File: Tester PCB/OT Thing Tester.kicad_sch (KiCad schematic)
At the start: 84 parts, among them J1 Conn_01x05, J2 Conn_01x08, J3 Conn_01x05, J4 Conn_01x05, J5 Link, J6 Link, Q1 BSP62, Q2 BSP62, Q3 BC847, Q4 BC847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

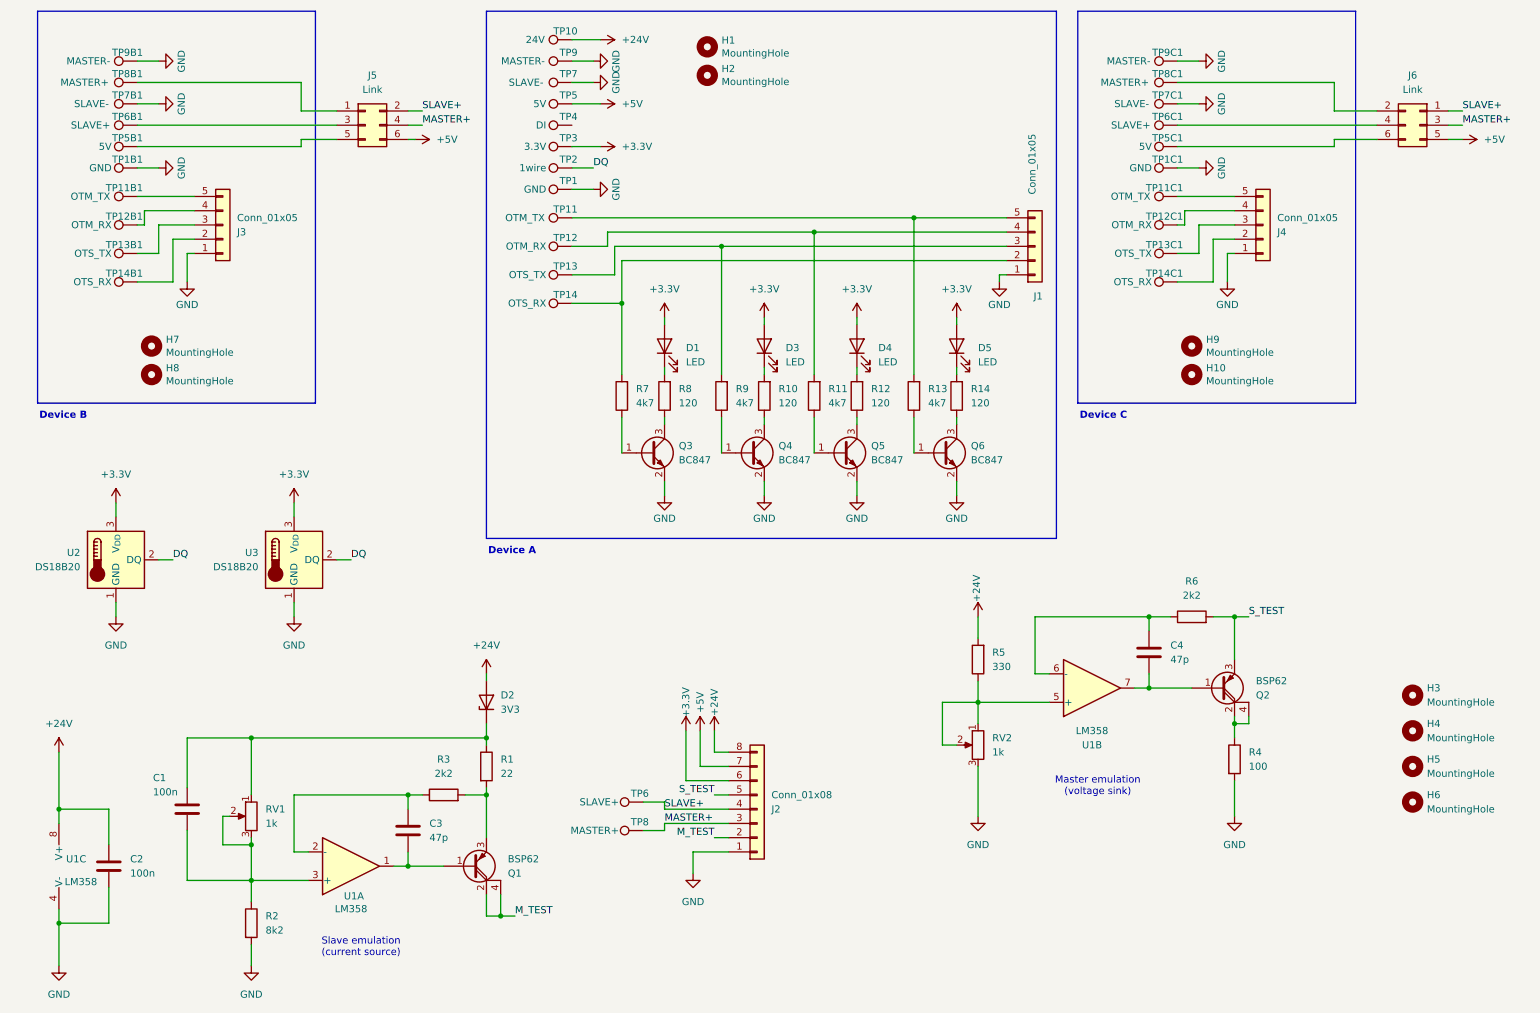
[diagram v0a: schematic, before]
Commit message: add USB test points single board test w/ power supply
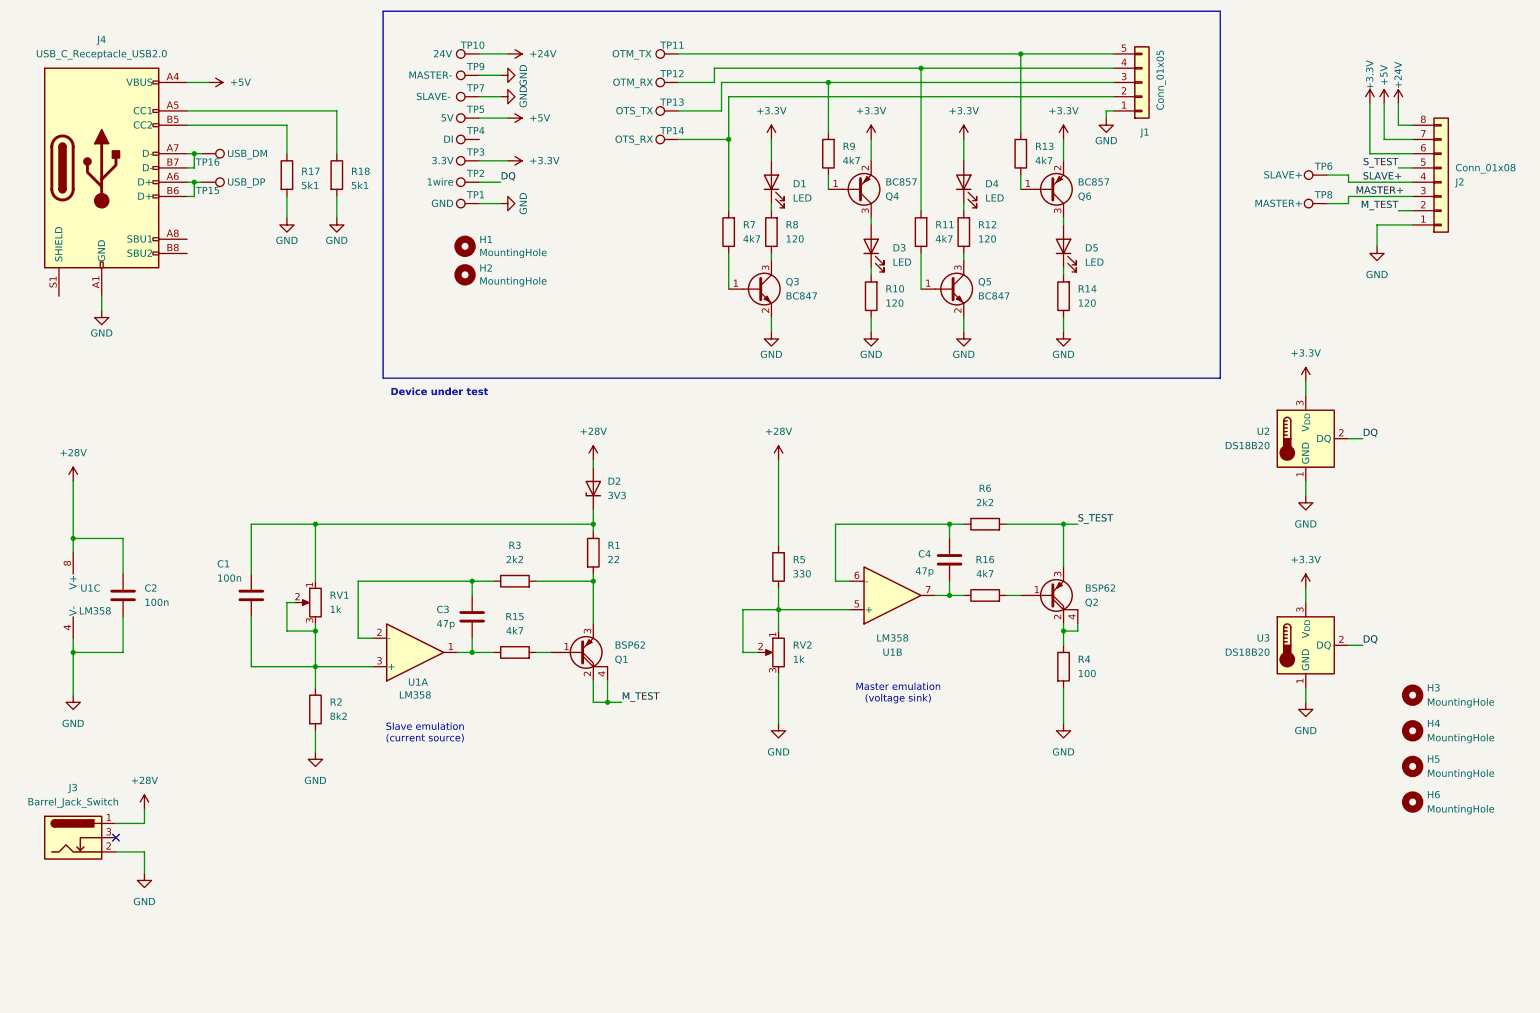
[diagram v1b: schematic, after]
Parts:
- removed H10, H7, H8, H9: MountingHole, MountingHole:MountingHole_2.7mm_M2.5, symbol Mechanical:MountingHole
- removed J3, J4: Conn_01x05, Connector_PinHeader_2.54mm:PinHeader_1x05_P2.54mm_Vertical, symbol Connector_Generic:Conn_01x05
- removed J5, J6: Link, Connector_PinHeader_2.54mm:PinHeader_2x03_P2.54mm_Vertical, symbol Connector_Generic:Conn_02x03_Odd_Even
- removed Q4, Q6: BC847, Package_TO_SOT_SMD:SOT-23, symbol Transistor_BJT:BC847
- removed TP11B1, TP11C1: OTM_TX, Library:TestPoint_THTPad_D2.0mm_Drill1.1mm, symbol Connector:TestPoint
- removed TP12B1, TP12C1: OTM_RX, Library:TestPoint_THTPad_D2.0mm_Drill1.1mm, symbol Connector:TestPoint
- removed TP13B1, TP13C1: OTS_TX, Library:TestPoint_THTPad_D2.0mm_Drill1.1mm, symbol Connector:TestPoint
- removed TP14B1, TP14C1: OTS_RX, Library:TestPoint_THTPad_D2.0mm_Drill1.1mm, symbol Connector:TestPoint
- removed TP1B1, TP1C1: GND, Library:TestPoint_THTPad_D2.0mm_Drill1.1mm, symbol Connector:TestPoint
- removed TP5B1, TP5C1: 5V, Library:TestPoint_THTPad_D2.0mm_Drill1.1mm, symbol Connector:TestPoint
- removed TP6B1, TP6C1: SLAVE+, Library:TestPoint_THTPad_D2.0mm_Drill1.1mm, symbol Connector:TestPoint
- removed TP7B1, TP7C1: SLAVE-, Library:TestPoint_THTPad_D2.0mm_Drill1.1mm, symbol Connector:TestPoint
- removed TP8B1, TP8C1: MASTER+, Library:TestPoint_THTPad_D2.0mm_Drill1.1mm, symbol Connector:TestPoint
- removed TP9B1, TP9C1: MASTER-, Library:TestPoint_THTPad_D2.0mm_Drill1.1mm, symbol Connector:TestPoint
- added J3: Barrel_Jack_Switch, Connector_BarrelJack:BarrelJack_GCT_DCJ200-10-A_Horizontal, symbol Connector:Barrel_Jack_Switch
- added J4: USB_C_Receptacle_USB2.0, Connector_USB:USB_C_Receptacle_HRO_TYPE-C-31-M-12, symbol Connector:USB_C_Receptacle_USB2.0
- added Q4, Q6: BC857, Package_TO_SOT_SMD:SOT-23, symbol Transistor_BJT:BC857
- added R15, R16: 4k7, Resistor_SMD:R_0805_2012Metric, symbol Device:R
- added R17, R18: 5k1, Resistor_SMD:R_0805_2012Metric, symbol Device:R
- added TP15: USB_DP, Library:TestPoint_THTPad_D2.0mm_Drill1.1mm, symbol Connector:TestPoint
- added TP16: USB_DM, Library:TestPoint_THTPad_D2.0mm_Drill1.1mm, symbol Connector:TestPoint
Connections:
- net +24V: no longer C2.1, D2.2 (A), R5.2, U1.8 (V+)
- net +3.3V: now also Q4.2 (E), Q6.2 (E); no longer D3.2 (A), D5.2 (A)
- net +5V: now also J4.A4 (VBUS), J4.A9 (VBUS), J4.B4 (VBUS), J4.B9 (VBUS)
- net GND: now also R10.1, R14.1, J3.2, J4.A1 (GND), J4.A12 (GND), J4.B1 (GND), J4.B12 (GND), R17.2, R18.2
- net at C4.2, U1.7: now also R16.1; no longer Q2.1 (B)
- net at R9.1: now also Q4.1 (B)
- net at C3.2, U1.1: now also R15.1; no longer Q1.1 (B)
- net at R13.1: now also Q6.1 (B)
- new net: J4.B5 (CC2), R17.1
- new net: D5.2 (A), Q6.3 (C)
- new net: D3.2 (A), Q4.3 (C)
- new net: Q2.1 (B), R16.2
- new net: J4.A5 (CC1), R18.1
- new net: J4.A6 (D+), J4.B6 (D+), TP15.1
- new net: J4.A7 (D-), J4.B7 (D-), TP16.1
- new net: Q1.1 (B), R15.2
- new net +28V: C2.1, D2.2 (A), J3.1, R5.2, U1.8 (V+)
- no-connect marks 0 -> 1
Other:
- note added: "Device under test"
- note removed: "Device A"
- note removed: "Device B"
- note removed: "Device C"
- moved on the sheet: C1, C2, C3, C4, D1, D2, D3, D4, D5, H1, H2, J1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
